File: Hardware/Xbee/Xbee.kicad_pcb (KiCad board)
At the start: 2 copper layers, 83 x 50 mm, 49 parts, among them J1 Alimentación, J2 Raspberry, J3 Pines 1, J4 Pines 2, J5 Programación, J6 Entrada, J7 Salida, J8 Batería, K1 SANYOU_SRD_Form_C, Q1 2N7002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

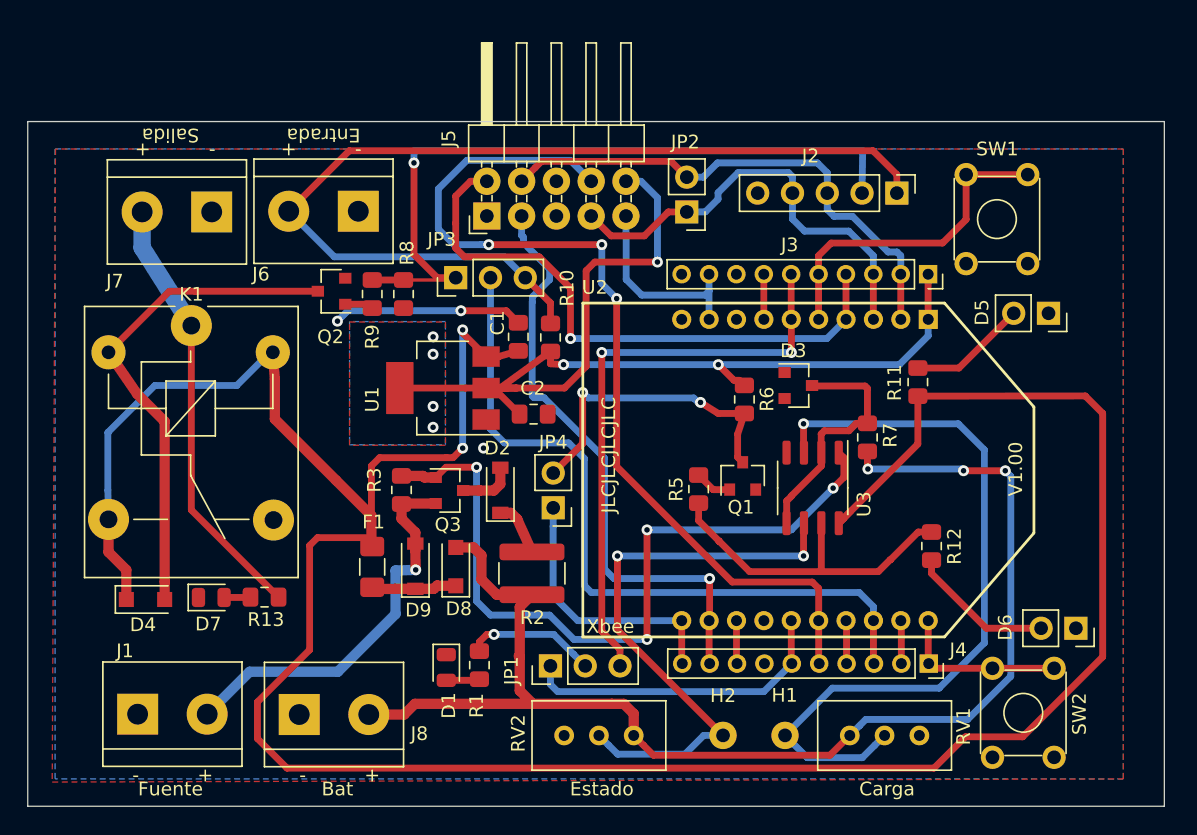
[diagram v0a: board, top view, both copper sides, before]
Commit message: Change footprints
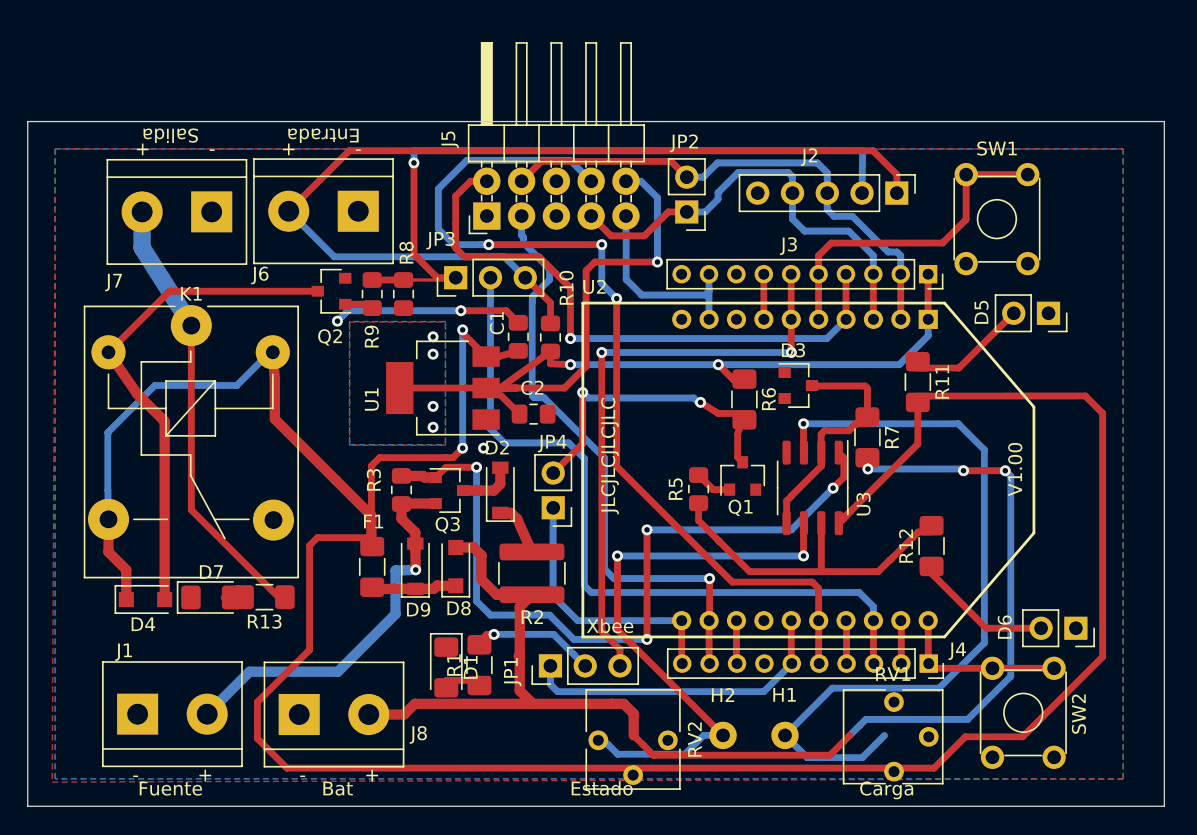
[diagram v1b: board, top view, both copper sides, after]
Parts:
- D1: value Blue Assoc-RSSI -> Green Assoc-RSSI; footprint LED_SMD:LED_0805_2012Metric -> LED_SMD:LED_1206_3216Metric_Pad1.42x1.75mm_HandSolder
- D5: value LED ON -> LED ON Verde
- D6: value LED Batería -> LED Batería Rojo
- D7: value LED Green Salida -> LED Blue Salida; footprint LED_SMD:LED_0805_2012Metric -> LED_SMD:LED_1206_3216Metric_Pad1.42x1.75mm_HandSolder
- R1, R11, R12, R6, R7: footprint Resistor_SMD:R_0805_2012Metric_Pad1.15x1.40mm_HandSolder -> Resistor_SMD:R_1206_3216Metric_Pad1.42x1.75mm_HandSolder
- R13: value 4k7 -> 1k; footprint Resistor_SMD:R_0805_2012Metric_Pad1.15x1.40mm_HandSolder -> Resistor_SMD:R_1206_3216Metric_Pad1.42x1.75mm_HandSolder
- RV1, RV2: footprint Potentiometer_THT:Potentiometer_Bourns_3386C_Horizontal -> Potentiometer_THT:Potentiometer_Vishay_T73YP_Vertical
- moved RV1 4.17 mm to (143.3, 77.5), turned to 0 degrees
- moved RV2 2.61 mm to (121.7, 75.2)

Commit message: Change footprints 2
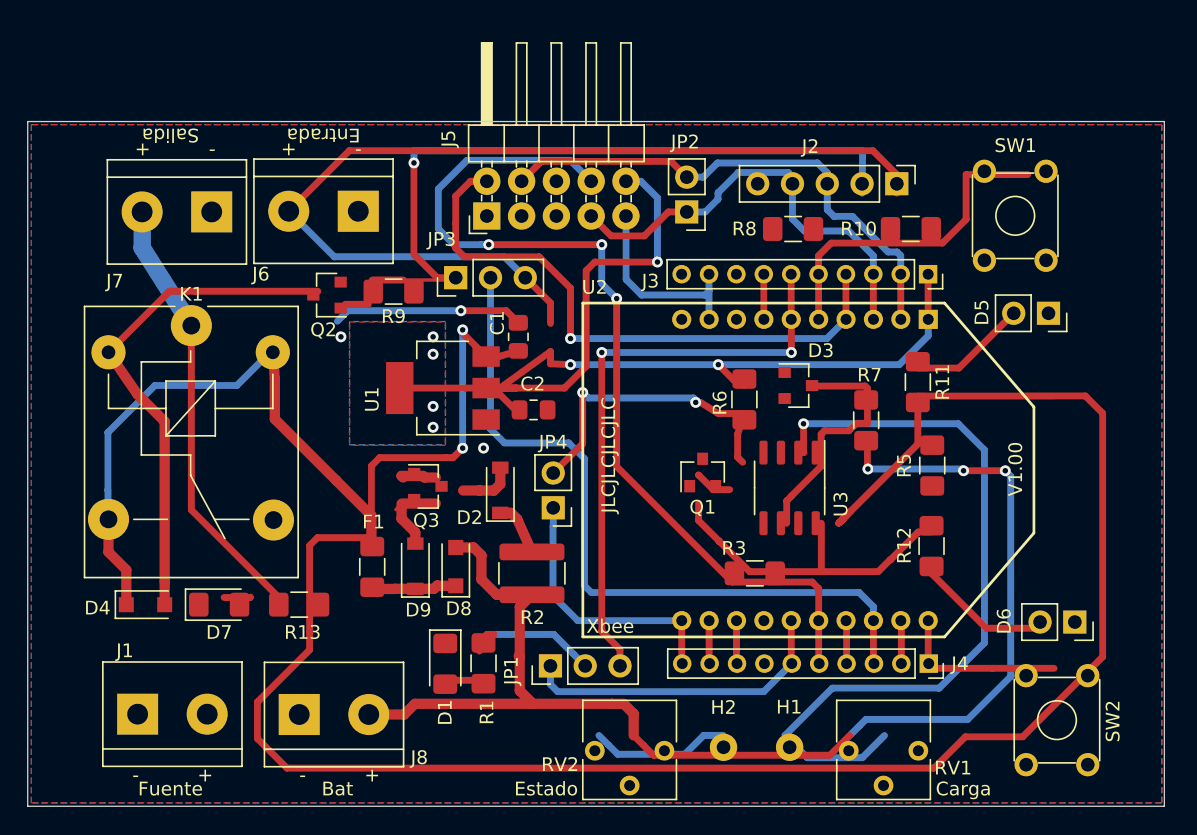
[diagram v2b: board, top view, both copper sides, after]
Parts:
- D2, D9: value DSU24 -> APD240
- R10, R3, R5, R8, R9: footprint Resistor_SMD:R_0805_2012Metric_Pad1.15x1.40mm_HandSolder -> Resistor_SMD:R_1206_3216Metric_Pad1.42x1.75mm_HandSolder
- moved R8 28.8 mm to (135.9, 37.8), turned to 180 degrees
- moved R10 27.5 mm to (144.5, 37.8), turned to 180 degrees
- moved R3 26.5 mm to (133.1, 63.0), turned to 0 degrees
- moved R5 17.1 mm to (146.1, 55.1)
- moved RV1 3.64 mm to (140.0, 75.9), turned to 270 degrees
- moved Q1 2.93 mm to (129.3, 55.6)
- moved R13 2.59 mm to (99.8, 65.3)
- moved SW2 2.52 mm to (152.9, 77.0)
- moved U3 1.68 mm to (135.6, 56.8)
- moved Q3 1.60 mm to (109.2, 56.6)
- moved R9 1.57 mm to (106.7, 42.4), turned to 180 degrees
- moved SW1 1.36 mm to (149.9, 40.1)
- moved R7 1.25 mm to (141.2, 51.8)
- moved H1 0.93 mm to (135.6, 75.7)
- moved H2 0.87 mm to (130.8, 75.7)
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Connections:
- R9 pad 1: Net-(Q2-Pad1) -> /DIO2-Salida
- R9 pad 2: /DIO2-Salida -> Net-(Q2-Pad1)
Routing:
- net /CargaBatería: track 55.5 -> 2.87 mm, vias 4 -> 0
- net /CTS: track 44.0 -> 3.15 mm, vias 1 -> 0
- net Net-(H2-Pad1): track 42.5 -> 10.2 mm, vias 2 -> 0
- net /Vin+: track 29.8 -> 6.41 mm, vias 1 -> 0
- net Net-(Q1-Pad1): track 2.72 -> 0.00 mm
- net GNDREF: track 13.9 -> 16.6 mm
- net /LED-Assoc-RSSI: vias 1 -> 0

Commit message: Footprints 3
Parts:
- added H3: MountingHole, MountingHole:MountingHole_3.2mm_M3, F.Cu at (81.8, 33.8)
- added H4: MountingHole, MountingHole:MountingHole_3.2mm_M3, F.Cu at (82.0, 76.7)
- added H5: MountingHole, MountingHole:MountingHole_3.2mm_M3, F.Cu at (159.8, 33.8)
- added H6: MountingHole, MountingHole:MountingHole_3.2mm_M3, F.Cu at (161.8, 77.5)
- C1, C2: footprint Capacitor_SMD:C_0805_2012Metric_Pad1.15x1.40mm_HandSolder -> Capacitor_SMD:C_1206_3216Metric_Pad1.42x1.75mm_HandSolder
- D4: value DSK26 -> MURA220; footprint Diode_SMD:D_SOD-123F -> Diode_SMD:D_SMA_Handsoldering
- D8: value DSK26 -> MURA220; footprint Diode_SMD:D_SOD-123F -> Diode_SMD:D_SMA
- J5: footprint Connector_PinHeader_2.54mm:PinHeader_2x05_P2.54mm_Horizontal -> Connector_PinSocket_2.54mm:PinSocket_2x05_P2.54mm_Horizontal
- K1: value SANYOU_SRD_Form_C -> ORWH-SH-112D1F
- moved J5 9.75 mm to (123.2, 36.1), turned to 270 degrees
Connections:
- SW1 pad 2: /RST -> GNDREF
- SW1 pad 3: GNDREF -> /RST
- SW2 pad 2: /Comm. -> GNDREF
- SW2 pad 3: GNDREF -> /Comm.

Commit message: SMD Routing
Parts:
- moved D6 33.9 mm to (141.2, 36.3), turned to 180 degrees
- moved D5 33.4 mm to (121.2, 43.8), turned to 180 degrees
- moved R12 22.3 mm to (128.3, 47.5), turned to 180 degrees
- moved R5 20.4 mm to (128.5, 65.5), turned to 180 degrees
- moved R11 17.3 mm to (128.3, 44.5), turned to 180 degrees
- moved R7 16.8 mm to (128.5, 62.7), turned to 0 degrees
- moved C1 16.1 mm to (120.3, 61.2), turned to 0 degrees
- moved D1 15.5 mm to (108.6, 54.2)
- moved JP2 15.5 mm to (115.6, 45.7), turned to 270 degrees
- moved C2 13.9 mm to (120.3, 64.5)
- moved JP4 11.6 mm to (121.9, 69.2), turned to 270 degrees
- moved D2 11.3 mm to (107.3, 48.3), turned to 180 degrees
- moved Q3 10.9 mm to (102.2, 48.3), turned to 180 degrees
- moved R10 9.92 mm to (134.6, 37.3)
- moved R1 9.01 mm to (105.0, 66.0), turned to 180 degrees
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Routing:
- net +12V: track 200.2 -> 99.3 mm, vias 2 -> 3
- net /Vin+: track 6.41 -> 105.1 mm, vias 0 -> 8
- net /CargaBatería: track 2.87 -> 80.9 mm, vias 0 -> 6
- net /CTS: track 3.15 -> 55.9 mm, vias 0 -> 3
- net /Bat-DIO4: track 22.9 -> 75.7 mm, vias 2 -> 4
- net /RSSI: track 43.0 -> 89.9 mm, vias 2 -> 3
- net /RXD: track 37.8 -> 78.8 mm, vias 0 -> 4
- net Net-(D6-Pad2): track 10.6 -> 46.0 mm, vias 0 -> 4
- net Net-(H2-Pad1): track 10.2 -> 42.7 mm, vias 0 -> 1
- net /DTR-DIO8: track 14.6 -> 40.0 mm, vias 0 -> 3
- net /EstadoBatería: track 24.6 -> 49.2 mm, vias 0 -> 3
- net /TXD: track 32.0 -> 56.3 mm, vias 0 -> 5
- net /Bat+: track 95.5 -> 72.0 mm, vias 3 -> 8
- net /DIO2-Entrada: track 71.7 -> 49.8 mm, vias 0 -> 4
- net Net-(Q1-Pad1): track 0.00 -> 21.5 mm, vias 0 -> 2
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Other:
- board size 83 x 50 mm -> 81.3 x 50 mm
